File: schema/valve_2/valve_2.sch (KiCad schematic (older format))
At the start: 121 parts, among them J1 DB37, J2 DB37, J3 DB9, K1 i2c-1, K2 i2c-2, P1 SETUP, P2 power-1, P3 power-2, P4 SWD-IAP, U1 74HC165, U10 L293, U11 L293, U12 L293, U13 L293, U14 MINI-USB-B, U15 NCP3063, U16 NCP3063, U2 74HC165, U3 74HC164, U4 74HC164, U5 74HC164, U6 74HC164, U7 L293, U8 L293, U9 L293, X1 8MHz

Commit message: Accelerometer schema is finished.
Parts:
- added C?: 220n, symbol C
- added C?: 10u, symbol C
- added C? (x2): 100n, symbol C
- added Q? (x2): MOS_N, symbol MOS_N
- added R? (x6): 10k, symbol R
- added R? (x2): 8k2, symbol R
- added U?: LM317, symbol LM317
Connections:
- net labels added: +1.8V, scl-1v8, sda-1v8
- wire segments 689 -> 751
- no-connect marks 19 -> 27
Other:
- moved on the sheet: ACC?

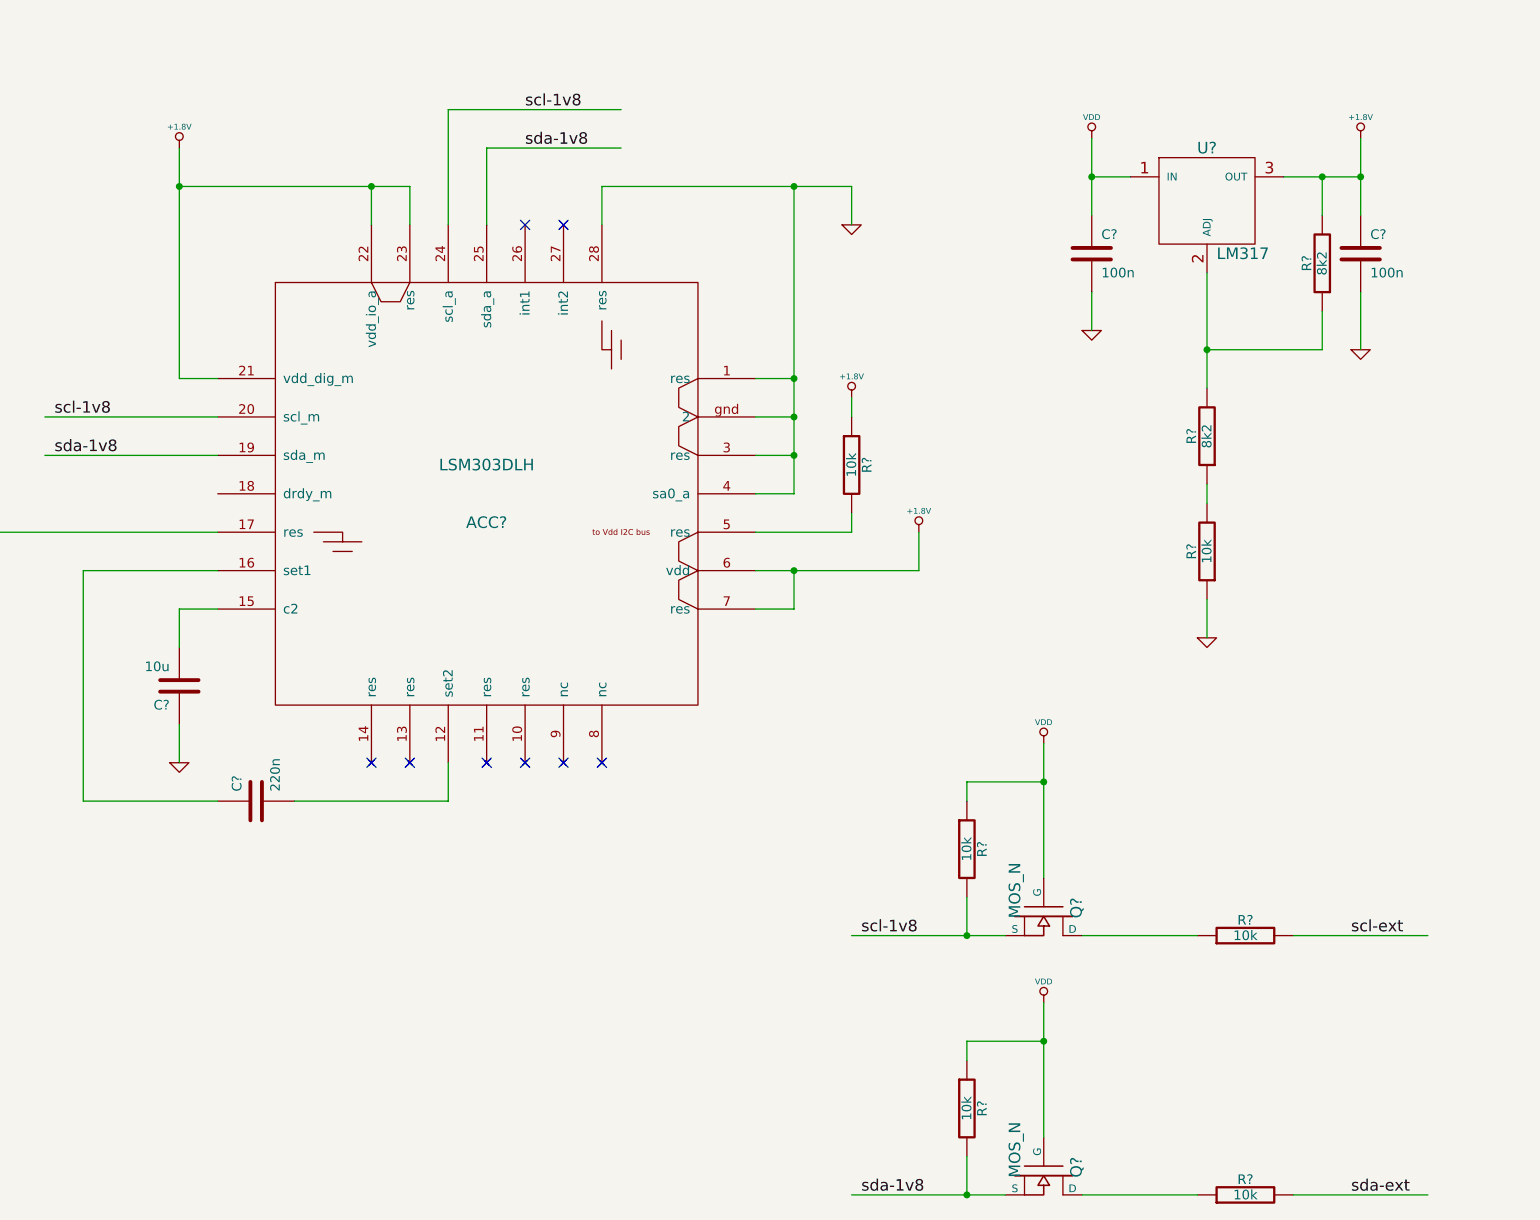
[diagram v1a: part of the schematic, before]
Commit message: Added LGA28 footprint.
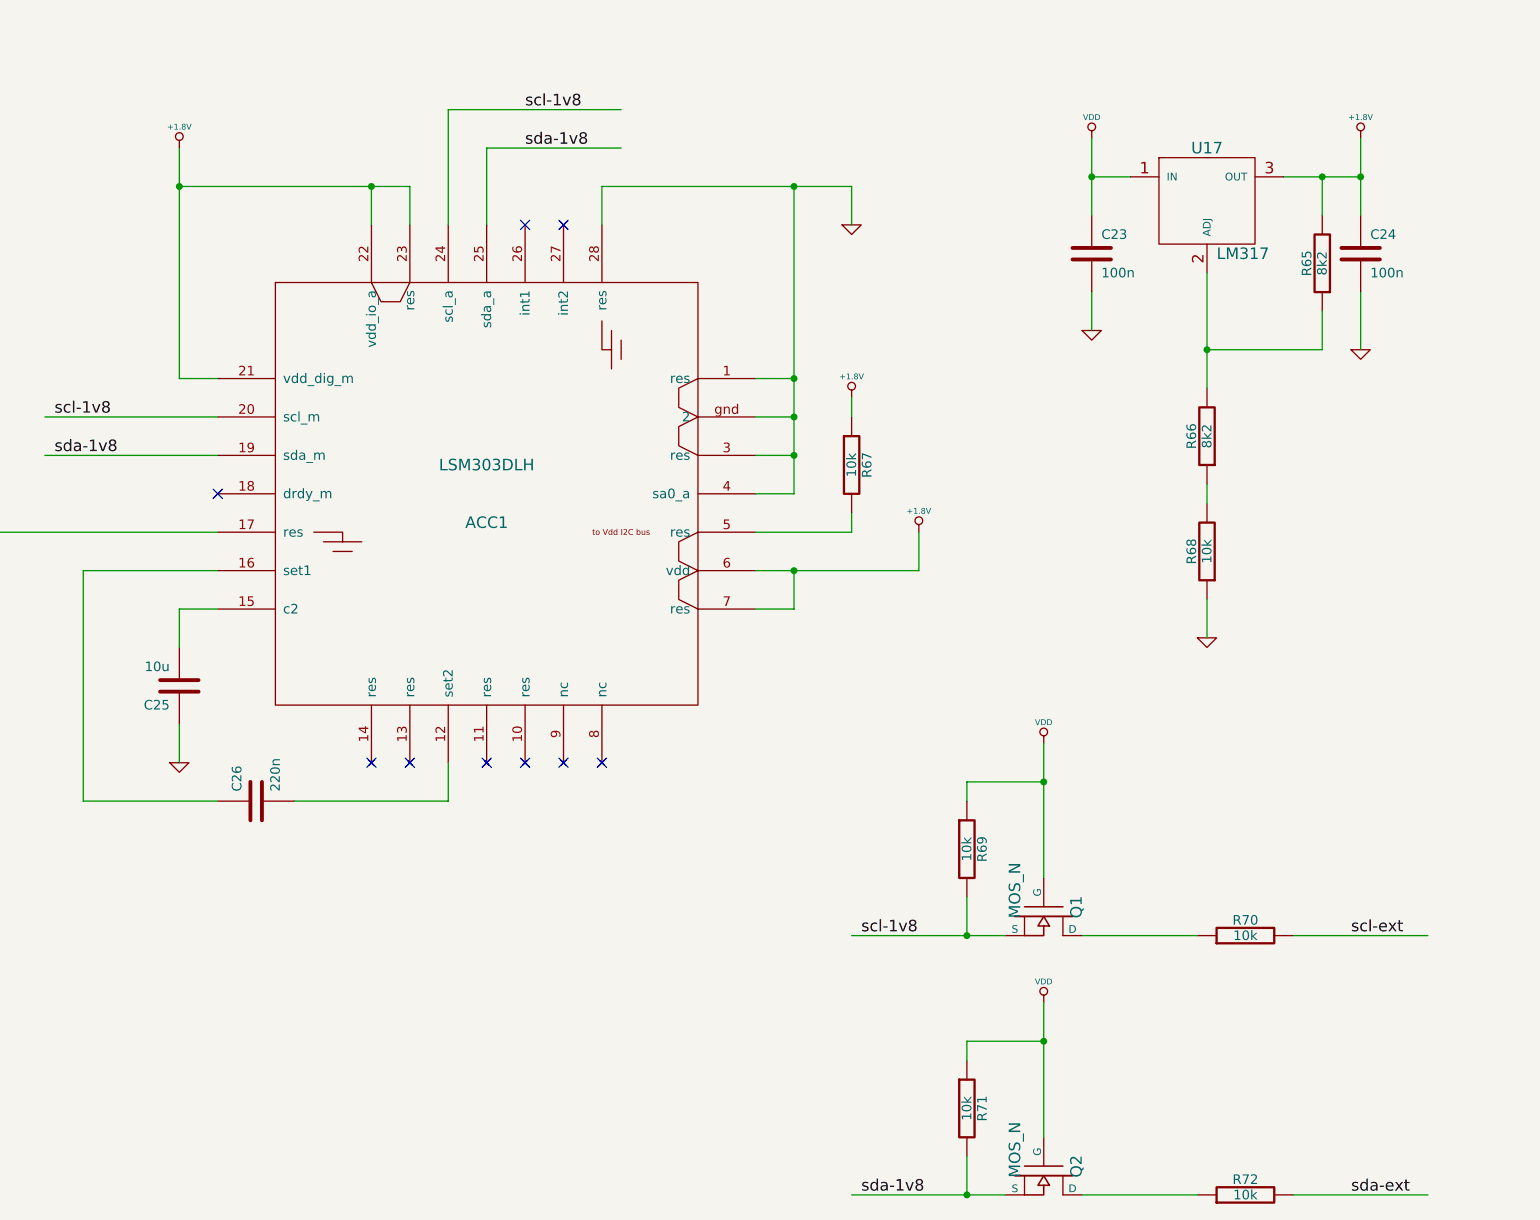
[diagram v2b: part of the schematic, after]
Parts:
- gave numbers to parts that had none: 16
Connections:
- no-connect marks 27 -> 28

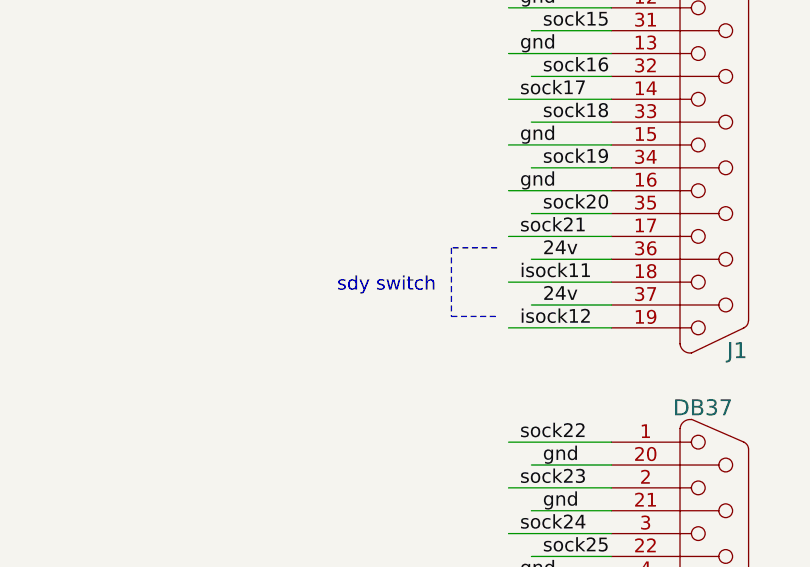
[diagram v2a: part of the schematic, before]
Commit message: Vavle and power cables for new schemas.
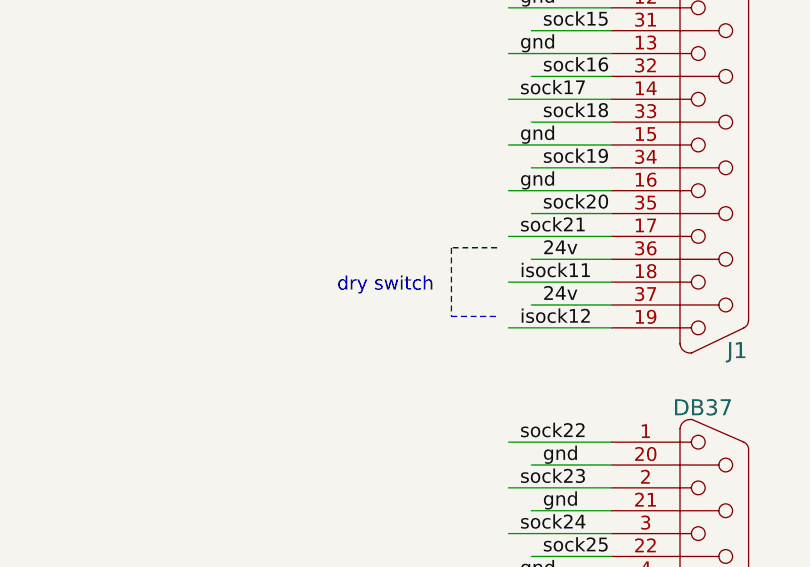
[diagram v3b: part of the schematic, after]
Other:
- note added: "dry switch\n"
- note removed: "sdy switch\n"
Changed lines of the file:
@@
-EESchema Schematic File Version 2  date Fri 28 Sep 2012 10:47:54 PM MSK
+EESchema Schematic File Version 2  date Wed 03 Oct 2012 07:07:06 PM MSK
 LIBS:power
 LIBS:device
@@
 Sheet 1 1
 Title ""
-Date "28 sep 2012"
+Date "3 oct 2012"
 Rev ""
 Comp ""
@@
 $EndComp
 Text Notes 9900 17750 0    60   ~ 0
-sdy switch\n
+dry switch\n
 Text Notes 9950 20250 0    60   ~ 0
 vac relay\n

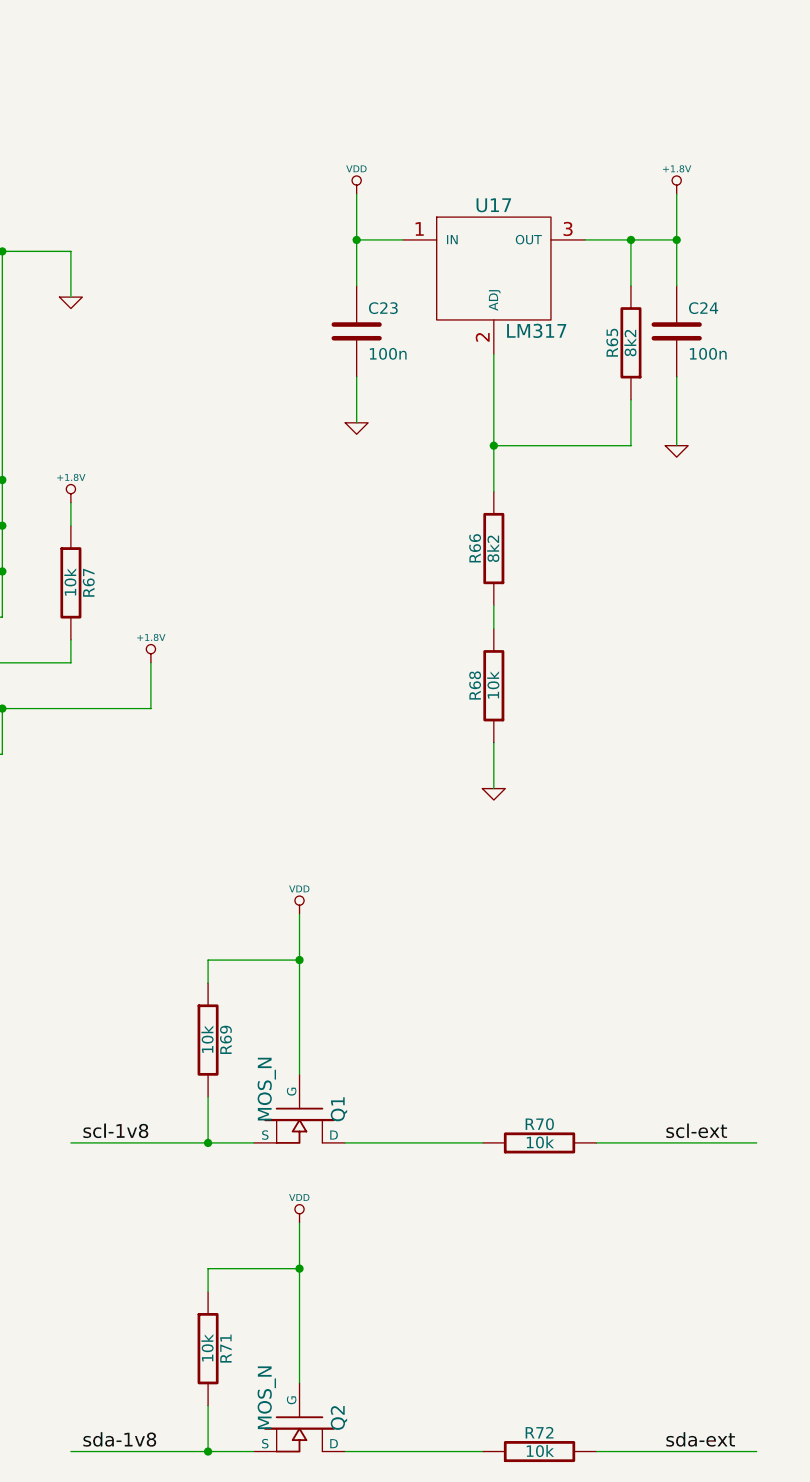
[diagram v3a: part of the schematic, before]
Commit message: Accelerometer lsm303... is inserted into PCB.
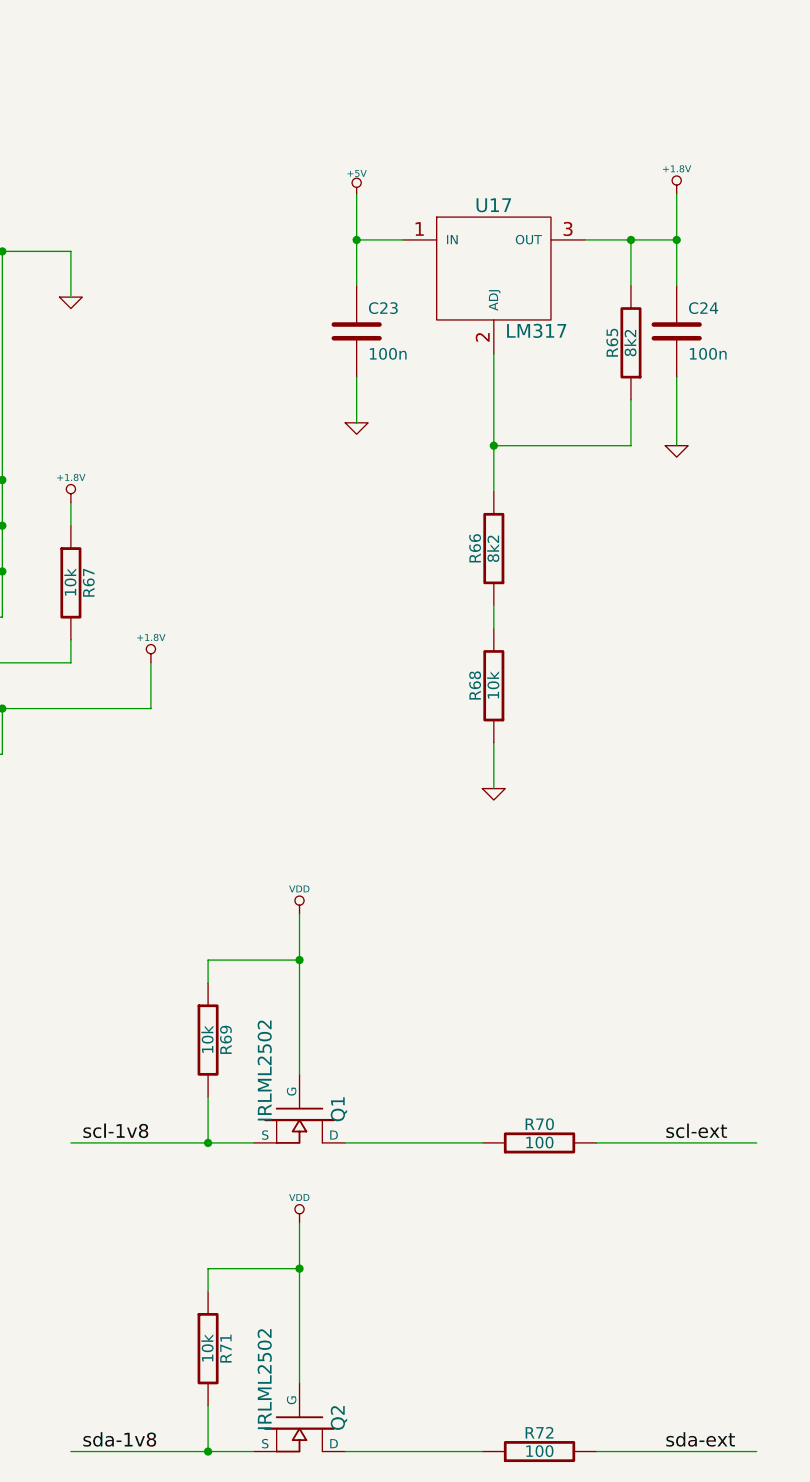
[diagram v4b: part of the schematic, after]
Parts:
- Q1, Q2: value MOS_N -> IRLML2502
- R70, R72: value 10k -> 100

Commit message: Made switchable USB.
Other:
- note added: "Actually USB- should be wired to \nVCC. And probably it would be \nbetter do dedicate a MCU pad for \nthis purpose to attach/detach USB."
- note added: "And here I should change powers. \nVss is digital and Vs is analog."
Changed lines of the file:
@@
-EESchema Schematic File Version 2  date Sat 13 Oct 2012 12:30:54 PM MSK
+EESchema Schematic File Version 2  date 22/11/2012 10:25:22
 LIBS:power
 LIBS:device
@@
 Sheet 1 1
 Title ""
-Date "13 oct 2012"
+Date "22 nov 2012"
 Rev ""
 Comp ""
@@
 Comment4 ""
 $EndDescr
-$Comp
-L +5V #PWR?
-U 1 1 507926A6
-P 20550 17000
-F 0 "#PWR?" H 20550 17090 20  0001 C CNN
-F 1 "+5V" H 20550 17090 30  0000 C CNN
-	1    20550 17000
-	1    0    0    -1
-$EndComp
-NoConn ~ 16000 18850
+Text Notes 16050 11950 0    60   ~ 0
+And here I should change powers. \nVss is digital and Vs is analog.
+Text Notes 950  16600 0    60   ~ 0
+Actually USB- should be wired to \nVCC. And probably it would be \nbetter do dedicate a MCU pad for \nthis purpose to attach/detach USB.
 Wire Wire Line
 	21150 18900 21150 18800
@@
 	21950 17800 21950 18100
 $Comp
+L +5V #PWR?
+U 1 1 507926A6
+P 20550 17000
+F 0 "#PWR?" H 20550 17090 20  0001 C CNN
+F 1 "+5V" H 20550 17090 30  0000 C CNN
+	1    20550 17000
+	1    0    0    -1
+$EndComp
+NoConn ~ 16000 18850
+$Comp
 L R R68
